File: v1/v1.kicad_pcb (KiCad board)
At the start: 2 copper layers, 101.5 x 88.1 mm, 45 parts, among them CON1 SNES-CONN, M1 LY68L6400SLIT, U1 SN74LV165APWR, U2 SN74LV165APWR, U3 SN74LV165APWR, U4 SN74LVC8T245PWR, U5 PIC12F629-I/SN, U6 AMS1117-3.3, U7 SN74LVC8T245PWR, U8 Pair of 20-pin 1.27mm pitch v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

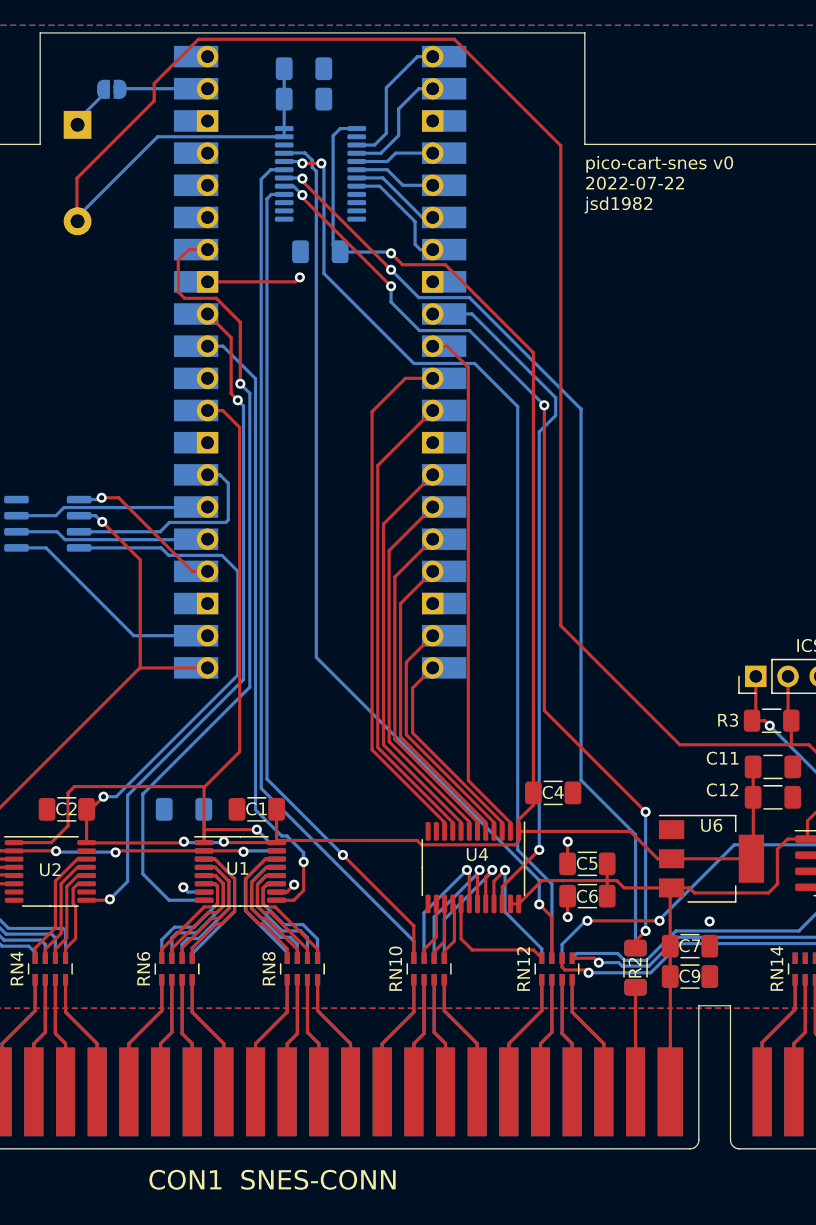
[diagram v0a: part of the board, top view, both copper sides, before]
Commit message: v1: replace Pico component with pair of pin headers
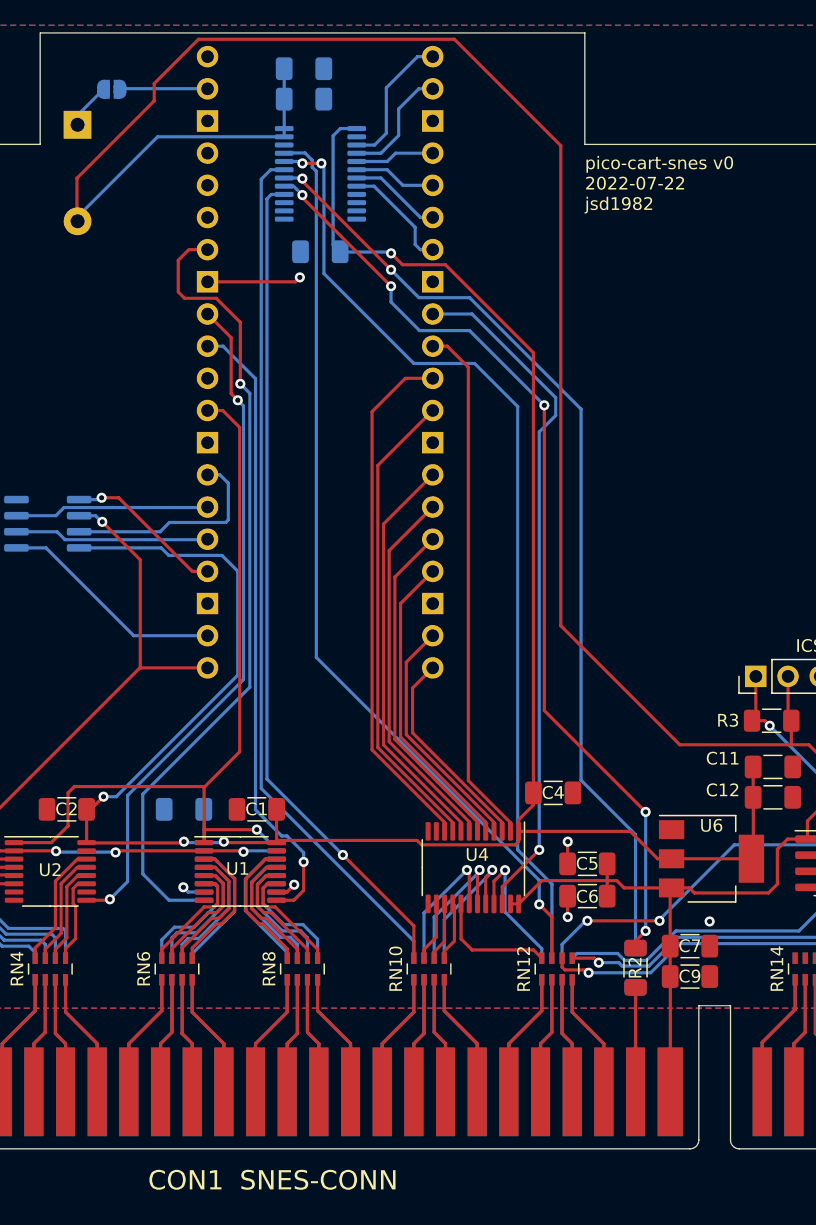
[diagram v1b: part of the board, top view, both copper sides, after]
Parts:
- removed U8: Pair of 20-pin 1.27mm pitch vertical pin headers, RP-Pico:RPi_Pico_SMD_TH
- added Pico1: Conn_01x20, Connector_PinHeader_2.54mm:PinHeader_1x20_P2.54mm_Vertical, B.Cu at (146.2, 47.6)
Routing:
- net /D~{OE}: track 52.6 -> 54.2 mm

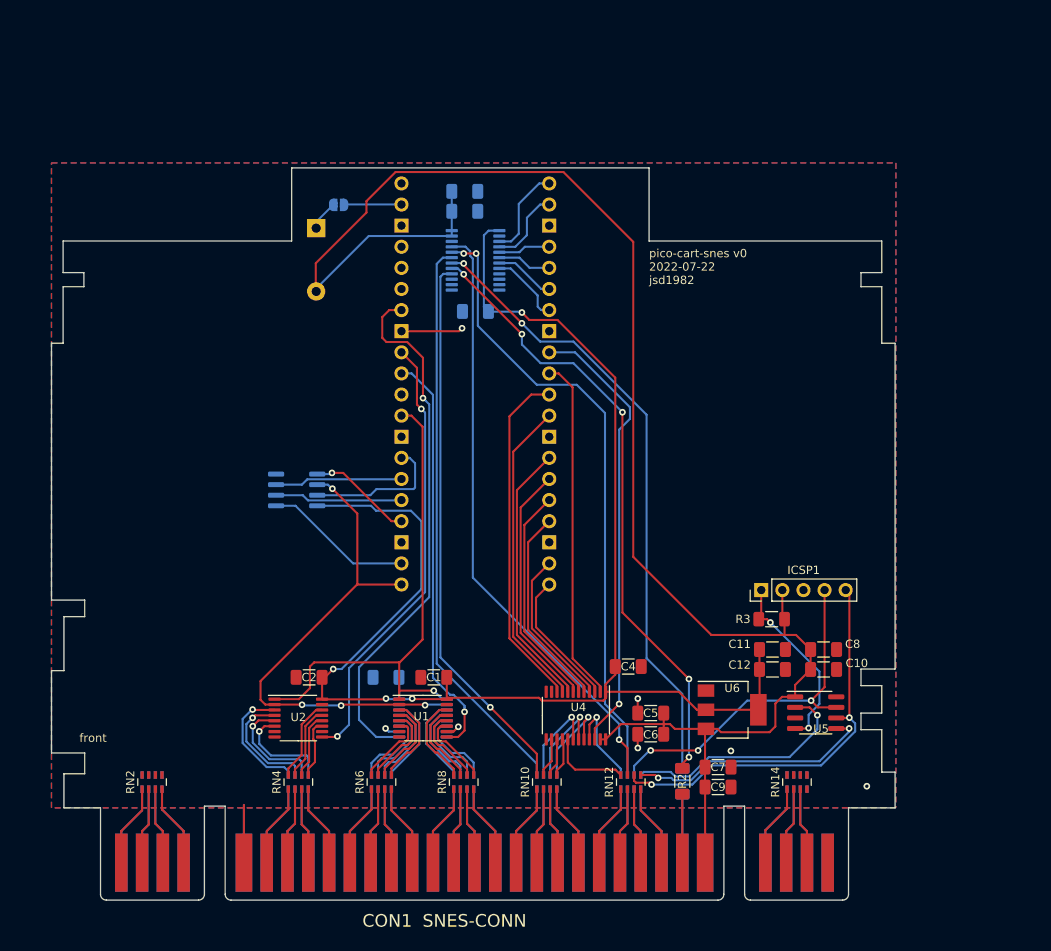
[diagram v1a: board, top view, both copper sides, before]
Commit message: v1: redo shift regs; redo gpio pin assignments; add jumpers for LDO vs Pico 3V3 power supply; use TXS0101 for /RESET
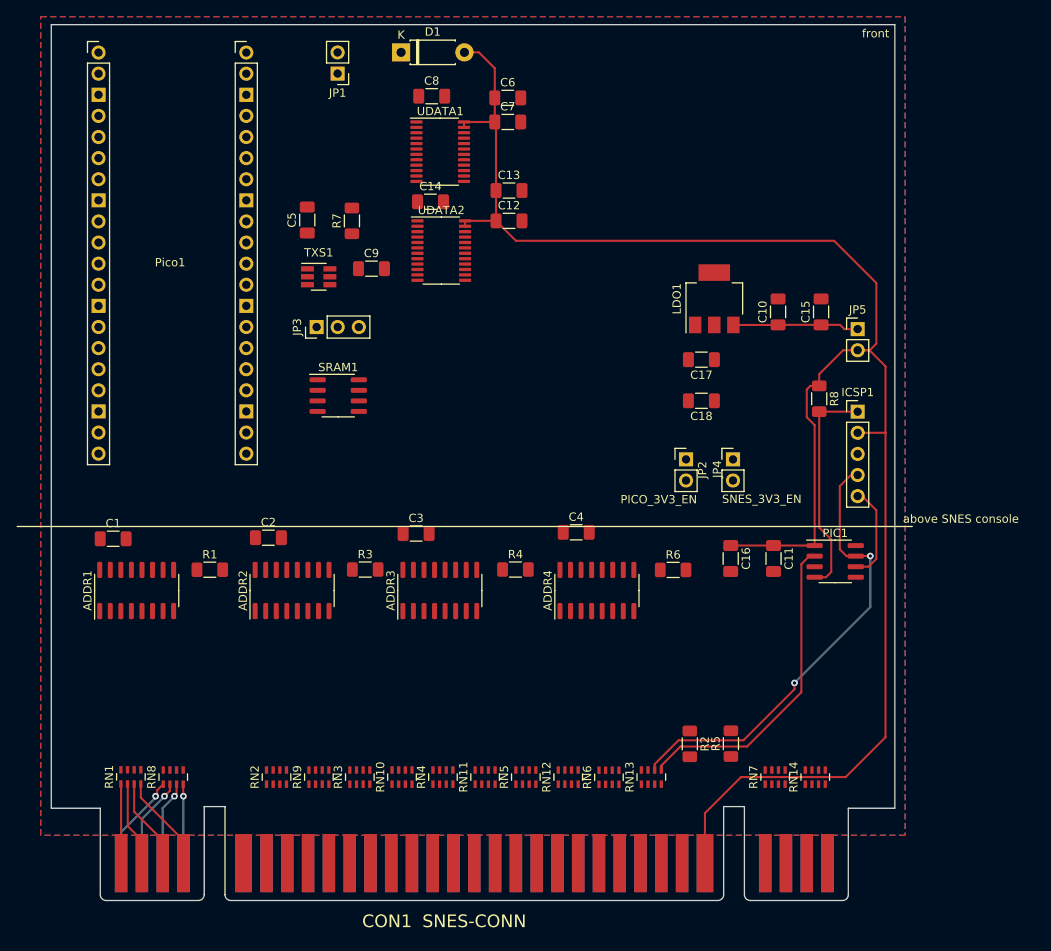
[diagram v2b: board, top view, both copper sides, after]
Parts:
- removed M1: LY68L6400SLIT, Package_SO:SOIC-8_3.9x4.9mm_P1.27mm
- removed U1, U2, U3: SN74LV165APWR, Package_SO:TSSOP-16_4.4x5mm_P0.65mm
- removed U4, U7: SN74LVC8T245PWR, Package_SO:TSSOP-24_4.4x7.8mm_P0.65mm
- removed U5: PIC12F629-I/SN, Package_SO:SOIC-8_3.9x4.9mm_P1.27mm
- removed U6: AMS1117-3.3, Package_TO_SOT_SMD:SOT-223-3_TabPin2
- added ADDR1: 74LV166A, Package_SO:SOIC-16_3.9x9.9mm_P1.27mm, F.Cu at (96.5, 96.5)
- added ADDR2: 74LV166A, Package_SO:SOIC-16_3.9x9.9mm_P1.27mm, F.Cu at (115.2, 96.5)
- added ADDR3: 74LV166A, Package_SO:SOIC-16_3.9x9.9mm_P1.27mm, F.Cu at (133.0, 96.5)
- added ADDR4: 74LV166A, Package_SO:SOIC-16_3.9x9.9mm_P1.27mm, F.Cu at (151.9, 96.5)
- added C16: 0.1uF, Capacitor_SMD:C_1206_3216Metric_Pad1.33x1.80mm_HandSolder, F.Cu at (168.0, 92.7)
- added C17: 10uF, Capacitor_SMD:C_1206_3216Metric_Pad1.33x1.80mm_HandSolder, F.Cu at (164.5, 68.8)
- added C18: 0.1uF, Capacitor_SMD:C_1206_3216Metric_Pad1.33x1.80mm_HandSolder, F.Cu at (164.5, 73.7)
- added JP2: PICO_3V3_EN, Connector_PinHeader_2.54mm:PinHeader_1x02_P2.54mm_Vertical, F.Cu at (162.7, 80.8)
- added JP3: CLK_OR_WRAM, Connector_PinHeader_2.54mm:PinHeader_1x03_P2.54mm_Vertical, F.Cu at (118.2, 64.8)
- added JP4: SNES_3V3_EN, Connector_PinHeader_2.54mm:PinHeader_1x02_P2.54mm_Vertical, F.Cu at (168.3, 80.8)
- added JP5: LDO_EN, Connector_PinHeader_2.54mm:PinHeader_1x02_P2.54mm_Vertical, F.Cu at (183.3, 65.1)
- added LDO1: AMS1117-3.3, Package_TO_SOT_SMD:SOT-223-3_TabPin2, F.Cu at (166.1, 61.5)
- added PIC1: PIC12F629-I/SN, Package_SO:SOIC-8_3.9x4.9mm_P1.27mm, F.Cu at (180.6, 93.0)
- added R4: 10kR, Resistor_SMD:R_1206_3216Metric_Pad1.30x1.75mm_HandSolder, F.Cu at (142.1, 94.0)
- added R5: 100R, Resistor_SMD:R_1206_3216Metric_Pad1.30x1.75mm_HandSolder, F.Cu at (168.1, 115.0)
- added R6: 10kR, Resistor_SMD:R_1206_3216Metric_Pad1.30x1.75mm_HandSolder, F.Cu at (161.1, 94.1)
- added R7: 10kR, Resistor_SMD:R_1206_3216Metric_Pad1.30x1.75mm_HandSolder, F.Cu at (122.5, 52.1)
- added R8: 10kR, Resistor_SMD:R_1206_3216Metric_Pad1.30x1.75mm_HandSolder, F.Cu at (178.7, 73.5)
- added SRAM1: LY68L6400SLIT, Package_SO:SOIC-8_3.9x4.9mm_P1.27mm, F.Cu at (120.8, 73.1)
- added TXS1: TXS0101, Package_TO_SOT_SMD:SOT-23-6_Handsoldering, F.Cu at (118.5, 58.8)
- added UDATA1: SN74LVC8T245PWR, Package_SO:TSSOP-24_4.4x7.8mm_P0.65mm, F.Cu at (133.1, 43.8)
- added UDATA2: SN74LVC8T245PWR, Package_SO:TSSOP-24_4.4x7.8mm_P0.65mm, F.Cu at (133.2, 55.6)
- C11: value 10uF -> 1uF
- C12: value 0.1uF -> 1uF
- C13, C14, C3, D1, RN1, RN11, RN13, RN3, RN5, RN7, RN9: moved to F.Cu
- C15: value 1uF -> 10uF; moved to F.Cu
- C8: value 1uF -> 0.1uF
- C9: value 10uF -> 0.1uF
- CON1: footprint sd2snes:SNESCART_EXT2_SMTUSB -> SNES:SNESCART_EXT2
- ICSP1: value Conn_01x05 -> PIC12_ICSP
- JP1: value SolderJumper_2_Open -> SNES 5V -> Pico; footprint Jumper:SolderJumper-2_P1.3mm_Open_RoundedPad1.0x1.5mm -> Connector_PinHeader_2.54mm:PinHeader_1x02_P2.54mm_Vertical; moved to F.Cu
- Pico1: value Conn_01x20 -> RPi_Pico_2x20; footprint Connector_PinHeader_2.54mm:PinHeader_1x20_P2.54mm_Vertical -> RPi_Pico:RPi_Pico_2x20; moved to F.Cu
- R1: value 100R -> 10kR; moved to F.Cu
- moved C7 81.6 mm to (141.2, 40.2)
- moved C8 81.6 mm to (132.1, 37.1)
- moved C6 78.5 mm to (141.2, 37.3), turned to 0 degrees
- moved C9 75.0 mm to (124.8, 57.8)
- moved C5 72.3 mm to (117.1, 52.0), turned to 90 degrees
- moved C12 62.6 mm to (141.3, 52.1)
- moved R1 62.3 mm to (105.3, 94.0), turned to 0 degrees
- moved Pico1 56.5 mm to (92.0, 31.8), turned to 0 degrees
- moved R3 49.3 mm to (124.0, 94.0), turned to 0 degrees
- moved C15 45.3 mm to (178.9, 63.0), turned to 90 degrees
- moved C10 43.4 mm to (173.7, 63.0), turned to 90 degrees
- moved C1 42.0 mm to (93.7, 90.3), turned to 0 degrees
- moved RN7 37.5 mm to (173.4, 119.0)
- moved RN8 35.0 mm to (101.0, 119.0)
- moved RN9 27.4 mm to (118.5, 119.0)
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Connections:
- C10 pad 1: +5V -> Net-(C10-Pad1)
- C11 pad 1: +3.3V -> +5V
- C12 pad 1: +3.3V -> +5V
- C13 pad 1: +3.3V -> +5V
- C14 pad 1: +5V -> +3.3V
- C15 pad 1: +5V -> Net-(C10-Pad1)
- C5 pad 1: +5V -> +3.3V
- C8 pad 1: +5V -> +3.3V
- Pico1 pad 1: /~{RD} -> /D0
- Pico1 pad 10: /DDIR -> /D7
- Pico1 pad 11: /D0 -> /ADDR1QH
- Pico1 pad 12: /D1 -> /ADDR2QH
- Pico1 pad 14: /D2 -> /ADDR3QH
- Pico1 pad 15: /D3 -> /ADDR4QH
- Pico1 pad 16: /D4 -> /PSRAM_SIO0
- Pico1 pad 17: /D5 -> /PSRAM_SIO1
- Pico1 pad 19: /D6 -> /PSRAM_SIO2
- Pico1 pad 2: /~{WR} -> /D1
- Pico1 pad 20: /D7 -> /PSRAM_SIO3
- Pico1 pad 21: /CLK_133MHZ -> /PSRAM_~{CE}
- Pico1 pad 22: /PSRAM_~{CE} -> /CLK_133MHZ
- Pico1 pad 24: /PSRAM_SIO0 -> /CLK_INH
- Pico1 pad 25: /PSRAM_SIO1 -> /~{ADDRLD}
- Pico1 pad 26: /PSRAM_SIO2 -> /DDIR
- Pico1 pad 27: /PSRAM_SIO3 -> Net-(JP3-Pad1)
- Pico1 pad 29: /U1~{LD} -> /~{RESET}
- Pico1 pad 31: /U1QH -> /~{RD}
- Pico1 pad 32: /U2QH -> /~{WR}
- Pico1 pad 34: /U3QH -> /~{CE}
- Pico1 pad 36: unconnected-(Pico1-Pad36) -> Net-(JP2-Pad1)
- Pico1 pad 4: /~{CE} -> /D2
- Pico1 pad 5: /CPU_CLK -> /D3
- Pico1 pad 6: /~{RESET} -> /D4
- Pico1 pad 7: /~{IRQ} -> /D5
- Pico1 pad 9: /D~{OE} -> /D6
- R1 pad 1: /XCPU_CLK -> Net-(ADDR1-Pad9)
- R1 pad 2: /YCPU_CLK -> +3.3V
- R3 pad 1: +5V -> Net-(ADDR2-Pad9)
- R3 pad 2: /ICSPVPP -> +3.3V
- RN1 pad 1: /X~{PAWR} -> /XCLK_21.477MHZ
- RN1 pad 2: /XPA7 -> /XEXPAND
- RN1 pad 3: /XREFRESH -> /XPA6
- RN1 pad 4: /X~{WRAM} -> /X~{PARD}
- RN1 pad 5: /Y~{WRAM} -> /Y~{PARD}
- RN1 pad 6: /YREFRESH -> /YPA6
- RN1 pad 7: /YPA7 -> /YEXPAND
- RN1 pad 8: /Y~{PAWR} -> /YCLK_21.477MHZ
- RN10 pad 1: /X~{IRQ} -> /XA16
- RN10 pad 2: /XD0 -> /XA17
- RN10 pad 3: /XD1 -> /XA18
- RN10 pad 4: /XD2 -> /XA19
- RN10 pad 5: /YD2 -> /YA19
- RN10 pad 6: /YD1 -> /YA18
- RN10 pad 7: /YD0 -> /YA17
- RN10 pad 8: /Y~{IRQ} -> /YA16
- RN11 pad 1: /XCIC_CLK -> /XA20
- RN11 pad 2: /XCIC_IN -> /XA21
- RN11 pad 3: /X~{WR} -> /XA22
- RN11 pad 4: /XD7 -> /XA23
- RN11 pad 5: /YD7 -> /YA23
- RN11 pad 6: /Y~{WR} -> /YA22
- RN11 pad 7: /CIC_IN -> /YA21
- RN11 pad 8: /CIC_CLK -> /YA20
- RN12 pad 1: /XD3 -> /X~{CE}
- RN12 pad 2: /X~{RD} -> /XD4
- RN12 pad 3: /XCIC_OUT -> /XD5
- RN12 pad 4: /XCIC_RST -> /XD6
- RN12 pad 5: /CIC_RST -> /YD6
- RN12 pad 6: /CIC_OUT -> /YD5
- RN12 pad 7: /Y~{RD} -> /YD4
- RN12 pad 8: /YD3 -> /Y~{CE}
- RN13 pad 1: unconnected-(RN13-Pad1) -> /XD7
- RN13 pad 2: /XPA5 -> /X~{WR}
- RN13 pad 3: /XPA3 -> /XCIC_IN
- RN13 pad 4: /XPA1 -> /XCIC_CLK
- RN13 pad 5: /YPA1 -> /CIC_CLK
- RN13 pad 6: /YPA3 -> /CIC_IN
- RN13 pad 7: /YPA5 -> /Y~{WR}
- RN13 pad 8: unconnected-(RN13-Pad8) -> /YD7
- RN14 pad 1: /XPA0 -> /XPA1
- RN14 pad 2: /XPA2 -> /XPA3
- RN14 pad 3: /XPA4 -> /XPA5
- RN14 pad 6: /YPA4 -> /YPA5
- RN14 pad 7: /YPA2 -> /YPA3
- RN14 pad 8: /YPA0 -> /YPA1
- RN2 pad 1: /XCLK_21.477MHZ -> /XA11
- RN2 pad 2: /XEXPAND -> /XA10
- RN2 pad 3: /XPA6 -> /XA9
- RN2 pad 4: /X~{PARD} -> /XA8
- RN2 pad 5: /Y~{PARD} -> /YA8
- RN2 pad 6: /YPA6 -> /YA9
- RN2 pad 7: /YEXPAND -> /YA10
- RN2 pad 8: /YCLK_21.477MHZ -> /YA11
- RN3 pad 1: /XA15 -> /XA7
- RN3 pad 2: /XA14 -> /XA6
- RN3 pad 3: /XA13 -> /XA5
- RN3 pad 4: /XA12 -> /XA4
- RN3 pad 5: /YA12 -> /YA4
- RN3 pad 6: /YA13 -> /YA5
- RN3 pad 7: /YA14 -> /YA6
- RN3 pad 8: /YA15 -> /YA7
- RN4 pad 1: /XA11 -> /XA3
- RN4 pad 2: /XA10 -> /XA2
- RN4 pad 3: /XA9 -> /XA1
- RN4 pad 4: /XA8 -> /XA0
- RN4 pad 5: /YA8 -> /YA0
- RN4 pad 6: /YA9 -> /YA1
- RN4 pad 7: /YA10 -> /YA2
- RN4 pad 8: /YA11 -> /YA3
- RN5 pad 1: /XA19 -> /X~{IRQ}
- RN5 pad 2: /XA18 -> /XD0
- RN5 pad 3: /XA17 -> /XD1
- RN5 pad 4: /XA16 -> /XD2
- RN5 pad 5: /YA16 -> /YD2
- RN5 pad 6: /YA17 -> /YD1
- RN5 pad 7: /YA18 -> /YD0
- RN5 pad 8: /YA19 -> /Y~{IRQ}
- RN6 pad 1: /XA7 -> /XD3
- RN6 pad 2: /XA6 -> /X~{RD}
- RN6 pad 3: /XA5 -> /XCIC_OUT
- RN6 pad 4: /XA4 -> /XCIC_RST
- RN6 pad 5: /YA4 -> /CIC_RST
- RN6 pad 6: /YA5 -> /CIC_OUT
- RN6 pad 7: /YA6 -> /Y~{RD}
- RN6 pad 8: /YA7 -> /YD3
- RN7 pad 1: /XA23 -> /XPA0
- RN7 pad 2: /XA22 -> /XPA2
- RN7 pad 3: /XA21 -> /XPA4
- RN7 pad 4: /XA20 -> unconnected-(RN7-Pad4)
- RN7 pad 5: /YA20 -> unconnected-(RN7-Pad5)
- RN7 pad 6: /YA21 -> /YPA4
- RN7 pad 7: /YA22 -> /YPA2
- RN7 pad 8: /YA23 -> /YPA0
- RN8 pad 1: /XA3 -> /X~{WRAM}
- RN8 pad 2: /XA2 -> /XREFRESH
- RN8 pad 3: /XA1 -> /XPA7
- RN8 pad 4: /XA0 -> /X~{PAWR}
- RN8 pad 5: /YA0 -> /Y~{PAWR}
- RN8 pad 6: /YA1 -> /YPA7
- RN8 pad 7: /YA2 -> /YREFRESH
- RN8 pad 8: /YA3 -> /Y~{WRAM}
- RN9 pad 1: /XD6 -> /XA12
- RN9 pad 2: /XD5 -> /XA13
- RN9 pad 3: /XD4 -> /XA14
- RN9 pad 4: /X~{CE} -> /XA15
- RN9 pad 5: /Y~{CE} -> /YA15
- RN9 pad 6: /YD4 -> /YA14
- RN9 pad 7: /YD5 -> /YA13
- RN9 pad 8: /YD6 -> /YA12
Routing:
- net +3.3V: track 175.3 -> 0.00 mm, vias 4 -> 0
- net /Y~{WR}: track 76.1 -> 0.00 mm, vias 2 -> 0
- net /YCPU_CLK: track 75.4 -> 0.00 mm, vias 2 -> 0
- net /Y~{RESET}: track 75.0 -> 0.00 mm, vias 5 -> 0
- net /Y~{RD}: track 73.3 -> 0.00 mm, vias 1 -> 0
- net /Y~{CE}: track 68.6 -> 0.00 mm
- net /Y~{IRQ}: track 66.3 -> 0.00 mm, vias 1 -> 0
- net /U3QH: track 64.1 -> 0.00 mm, vias 1 -> 0
- net /CLK_133MHZ: track 61.7 -> 0.00 mm, vias 4 -> 0
- net /U1~{LD}: track 61.1 -> 0.00 mm, vias 1 -> 0
- net /D~{OE}: track 54.2 -> 0.00 mm, vias 1 -> 0
- net /U2QH: track 53.6 -> 0.00 mm, vias 2 -> 0
- net /U1QH: track 49.5 -> 0.00 mm, vias 1 -> 0
- net /DDIR: track 41.5 -> 0.00 mm
- net /D0: track 41.4 -> 0.00 mm
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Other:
- board size 101.5 x 88.1 mm -> 101.5 x 105.4 mm
- board text removed: "back"
- board text removed: "front"
- board text removed: "pico-cart-snes v0 2022-07-22 jsd1982"

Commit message: v1: fixed /WRAM vs CPU_CLK jumper selector to make sense; lots of PCB routing decisions
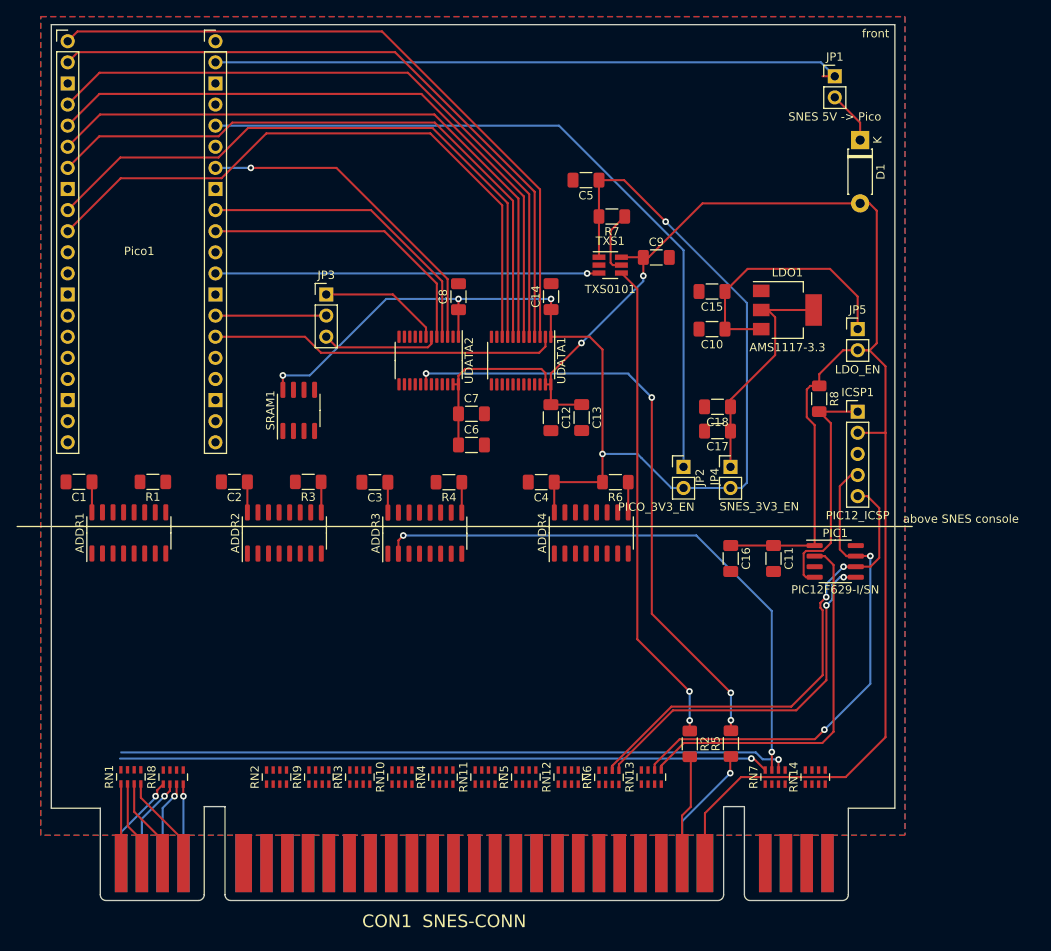
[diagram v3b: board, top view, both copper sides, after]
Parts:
- moved JP1 59.8 mm to (180.6, 34.7), turned to 0 degrees
- moved D1 56.2 mm to (183.6, 42.4), turned to -90 degrees
- moved C6 42.0 mm to (136.8, 79.0)
- moved C7 35.4 mm to (136.8, 75.3)
- moved TXS1 35.1 mm to (153.5, 57.4)
- moved C9 34.3 mm to (159.1, 56.5)
- moved C5 33.9 mm to (150.6, 47.2), turned to 180 degrees
- moved R7 31.3 mm to (153.7, 51.5), turned to 180 degrees
- moved C13 28.7 mm to (150.1, 75.7), turned to -90 degrees
- moved UDATA1 27.0 mm to (142.8, 68.9), turned to -90 degrees
- moved C8 24.3 mm to (135.3, 61.2), turned to 90 degrees
- moved C12 24.2 mm to (146.4, 75.8), turned to -90 degrees
- moved C14 18.5 mm to (146.4, 61.2), turned to 90 degrees
- moved C15 13.4 mm to (165.8, 60.6), turned to 180 degrees
- moved UDATA2 13.3 mm to (131.7, 68.9), turned to -90 degrees
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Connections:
- JP3 pad 1: Net-(JP3-Pad1) -> /~{WRAM}
- JP3 pad 2: /CPU_CLK -> Net-(JP3-Pad2)
- JP3 pad 3: /~{WRAM} -> /CPU_CLK
- Pico1 pad 27: Net-(JP3-Pad1) -> Net-(JP3-Pad2)
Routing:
- net +3.3V: track 0.00 -> 164.4 mm, vias 0 -> 5
- net Net-(JP2-Pad1): track 0.00 -> 88.6 mm
- net /D0: track 0.00 -> 82.9 mm
- net /D1: track 0.00 -> 81.1 mm
- net /YPA4: track 0.00 -> 80.7 mm, vias 0 -> 1
- net /D2: track 0.00 -> 80.3 mm
- net /D3: track 0.00 -> 78.5 mm
- net /YPA0: track 0.00 -> 78.2 mm, vias 0 -> 1
- net /D6: track 0.00 -> 76.9 mm
- net Net-(JP1-Pad1): track 0.00 -> 76.7 mm
- net /D4: track 0.00 -> 76.7 mm
- net /D7: track 0.00 -> 76.6 mm
- net /D5: track 0.00 -> 76.1 mm
- net /YCPU_CLK: track 0.00 -> 73.6 mm, vias 0 -> 4
- net /YPA2: track 0.00 -> 69.7 mm, vias 0 -> 2
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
